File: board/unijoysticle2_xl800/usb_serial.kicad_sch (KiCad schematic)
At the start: 12 parts, among them J1 USB_B_Micro, U2 AMS1117-3.3, U3 CH340C

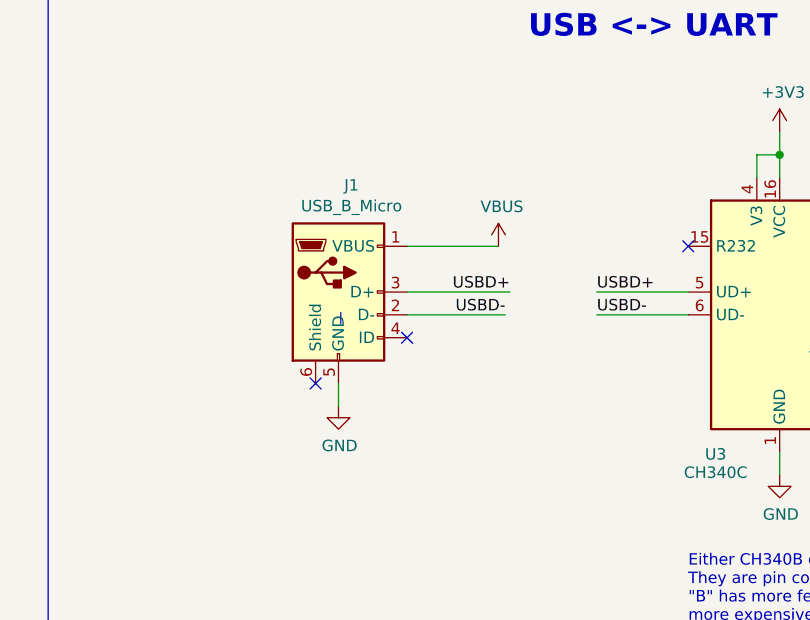
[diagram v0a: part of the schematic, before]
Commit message: 800xl: routes added
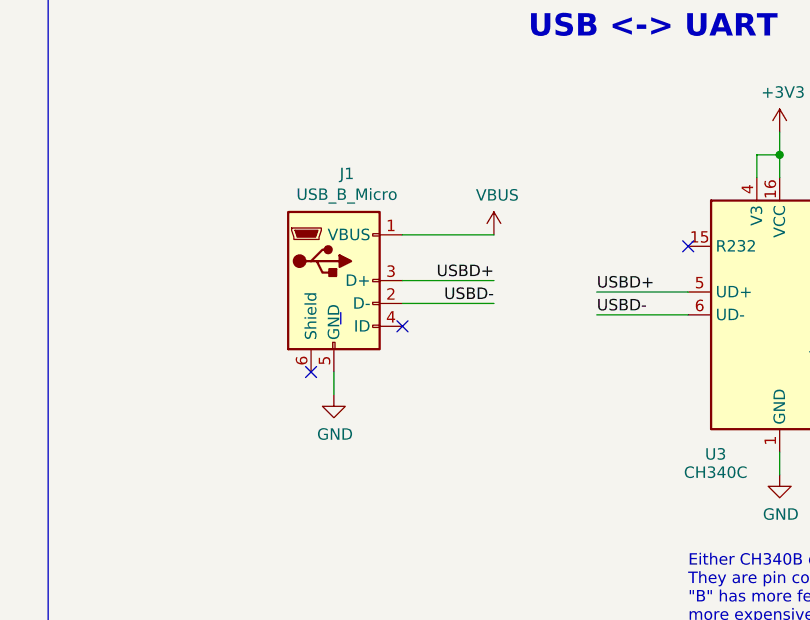
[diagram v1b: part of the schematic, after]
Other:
- title: Unijoysticle 2 A500 -> Unijoysticle 2 XL800
- moved on the sheet: J1
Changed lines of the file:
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@@
   (paper "A4")
   (title_block
-    (title "Unijoysticle 2 A500")
-    (date "2022-04-25")
+    (title "Unijoysticle 2 XL800")
+    (date "2023-06-16")
     (rev "A")
     (company "Ricardo Quesada")
@@
   (no_connect (at 204.47 52.07))
   (no_connect (at 204.47 54.61))
-  (no_connect (at 152.908 52.07))
+  (no_connect (at 152.4 50.8))
   (no_connect (at 184.15 41.91))
-  (no_connect (at 142.748 57.15))
+  (no_connect (at 142.24 55.88))
   (wire (pts (xy 73.66 55.88) (xy 73.66 57.15))
     (stroke (width 0) (type default))
@@
     (stroke (width 0) (type default))
   )
-  (wire (pts (xy 145.288 57.15) (xy 145.288 59.69))
+  (wire (pts (xy 144.78 58.42) (xy 144.78 55.88))
     (stroke (width 0) (type default))
   )
@@
     (stroke (width 0) (type default))
   )
-  (wire (pts (xy 152.908 41.91) (xy 163.068 41.91))
-    (stroke (width 0) (type default))
-  )
-  (wire (pts (xy 152.908 49.53) (xy 163.83 49.53))
+  (wire (pts (xy 152.4 48.26) (xy 162.56 48.26))
     (stroke (width 0) (type default))
   )
@@
     (stroke (width 0) (type default))
   )
-  (wire (pts (xy 152.908 46.99) (xy 164.338 46.99))
+  (wire (pts (xy 152.4 45.72) (xy 162.56 45.72))
     (stroke (width 0) (type default))
   )
@@
   )
   (wire (pts (xy 46.99 48.26) (xy 53.34 48.26))
+    (stroke (width 0) (type default))
+  )
+  (wire (pts (xy 152.4 40.64) (xy 162.56 40.64))
     (stroke (width 0) (type default))
   )
@@
     (effects (font (size 2.4892 2.4892) (thickness 0.4978) bold) (justify left bottom))
   )
-  (label "USBD-" (at 163.83 49.53 180) (fields_autoplaced)
+  (label "USBD-" (at 162.56 48.26 180) (fields_autoplaced)
     (effects (font (size 1.27 1.27)) (justify right bottom))
   )
@@
     (effects (font (size 1.27 1.27)) (justify left bottom))
   )
-  (label "USBD+" (at 164.338 46.99 180) (fields_autoplaced)
+  (label "USBD+" (at 162.56 45.72 180) (fields_autoplaced)
     (effects (font (size 1.27 1.27)) (justify right bottom))
   )
@@
     )
   )
-  (symbol (lib_id "power:VBUS") (at 163.068 41.91 0) (unit 1)
-    (in_bom yes) (on_board yes) (dnp no)
-    (property "Reference" "#PWR019" (at 163.068 45.72 0)
-      (effects (font (size 1.27 1.27)) hide)
-    )
-    (property "Value" "VBUS" (at 163.449 37.5158 0)
-      (effects (font (size 1.27 1.27)))
-    )
-    (property "Footprint" "" (at 163.068 41.91 0)
-      (effects (font (size 1.27 1.27)) hide)
-    )
-    (property "Datasheet" "" (at 163.068 41.91 0)
+  (symbol (lib_id "power:VBUS") (at 162.56 40.64 0) (unit 1)
+    (in_bom yes) (on_board yes) (dnp no)
+    (property "Reference" "#PWR019" (at 162.56 44.45 0)
+      (effects (font (size 1.27 1.27)) hide)
+    )
+    (property "Value" "VBUS" (at 162.941 36.2458 0)
+      (effects (font (size 1.27 1.27)))
+    )
+    (property "Footprint" "" (at 162.56 40.64 0)
+      (effects (font (size 1.27 1.27)) hide)
+    )
+    (property "Datasheet" "" (at 162.56 40.64 0)
       (effects (font (size 1.27 1.27)) hide)
     )
@@
     )
   )
-  (symbol (lib_id "power:GND") (at 145.288 59.69 0) (unit 1)
-    (in_bom yes) (on_board yes) (dnp no)
-    (property "Reference" "#PWR018" (at 145.288 66.04 0)
-      (effects (font (size 1.27 1.27)) hide)
-    )
-    (property "Value" "GND" (at 145.415 64.0842 0)
-      (effects (font (size 1.27 1.27)))
-    )
-    (property "Footprint" "" (at 145.288 59.69 0)
-      (effects (font (size 1.27 1.27)) hide)
-    )
-    (property "Datasheet" "" (at 145.288 59.69 0)
+  (symbol (lib_id "power:GND") (at 144.78 58.42 0) (unit 1)
+    (in_bom yes) (on_board yes) (dnp no)
+    (property "Reference" "#PWR018" (at 144.78 64.77 0)
+      (effects (font (size 1.27 1.27)) hide)
+    )
+    (property "Value" "GND" (at 144.907 62.8142 0)
+      (effects (font (size 1.27 1.27)))
+    )
+    (property "Footprint" "" (at 144.78 58.42 0)
+      (effects (font (size 1.27 1.27)) hide)
+    )
+    (property "Datasheet" "" (at 144.78 58.42 0)
       (effects (font (size 1.27 1.27)) hide)
     )
@@
     )
   )
-  (symbol (lib_id "Connector:USB_B_Micro") (at 145.288 46.99 0) (unit 1)
-    (in_bom yes) (on_board yes) (dnp no)
-    (property "Reference" "J1" (at 146.7358 35.1282 0)
-      (effects (font (size 1.27 1.27)))
-    )
-    (property "Value" "USB_B_Micro" (at 146.7358 37.4396 0)
-      (effects (font (size 1.27 1.27)))
-    )
-    (property "Footprint" "Connector_USB:USB_Micro-B_Amphenol_10118194_Horizontal" (at 149.098 48.26 0)
-      (effects (font (size 1.27 1.27)) hide)
-    )
-    (property "Datasheet" "~" (at 149.098 48.26 0)
-      (effects (font (size 1.27 1.27)) hide)
-    )
-    (property "LCSC" "" (at 145.288 46.99 0)
-      (effects (font (size 1.27 1.27)) hide)
-    )
+  (symbol (lib_id "Connector:USB_B_Micro") (at 144.78 45.72 0) (unit 1)
+    (in_bom yes) (on_board yes) (dnp no)
+    (property "Reference" "J1" (at 146.2278 33.8582 0)
+      (effects (font (size 1.27 1.27)))
+    )
+    (property "Value" "USB_B_Micro" (at 146.2278 36.1696 0)
+      (effects (font (size 1.27 1.27)))
+    )
+    (property "Footprint" "Connector_USB:USB_Micro-B_Amphenol_10118194_Horizontal" (at 148.59 46.99 0)
+      (effects (font (size 1.27 1.27)) hide)
+    )
+    (property "Datasheet" "~" (at 148.59 46.99 0)
+      (effects (font (size 1.27 1.27)) hide)
+    )
+    (property "LCSC" "" (at 144.78 45.72 0)
+      (effects (font (size 1.27 1.27)) hide)
+    )
